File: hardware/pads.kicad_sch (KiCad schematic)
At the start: 0 parts

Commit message: schematic: rx (ESP32-PICO-V3 + SX1281 + Wi-Fi antenna + boot button), blackbox and osd sheets drawn
Co-Authored-By: Claude Opus 5.5 <noreply@anthropic.com>
Claude-Session: https://claude.ai/code/session_01RFaS5jnC9tnPam9GBgmGnG
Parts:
- added D7: TPD2EUSB30, lib:TI_SOT-9X3-3_DRT, symbol lib:TPD2EUSB30DRTR
- added H1, H2, H3: MountingHole 3.5, lib:MountingHole_3.5mm_Ear_Flange5.2, symbol Mechanical:MountingHole
- added J10: M3, lib:MotorPad_PicoBlade_1x03_P1.25mm_PTH0.5, symbol lib:Molex_53047-0310
- added J13: M4, lib:MotorPad_PicoBlade_1x03_P1.25mm_PTH0.5, symbol lib:Molex_53047-0310
- added J16: TP0, lib:SolderPad_1.0x1.2mm, symbol Connector_Generic:Conn_01x01
- added J17: RP0, lib:SolderPad_1.0x1.2mm, symbol Connector_Generic:Conn_01x01
- added J18, J24: 5V, lib:SolderPad_1.0x1.2mm, symbol Connector_Generic:Conn_01x01
- added J19, J25, J27: GND, lib:SolderPad_1.0x1.2mm, symbol Connector_Generic:Conn_01x01
- added J2: +, lib:BattPad_3.0x2.0mm_PTH1.1, symbol Connector_Generic:Conn_01x01
- added J20: LED, lib:SolderPad_1.0x1.2mm_Dense, symbol Connector_Generic:Conn_01x01
- added J21: 5V, lib:SolderPad_1.0x1.2mm_Dense, symbol Connector_Generic:Conn_01x01
- added J22: BZ-, lib:SolderPad_1.0x1.2mm_Dense, symbol Connector_Generic:Conn_01x01
- added J23: CAM, lib:SolderPad_1.0x1.2mm, symbol Connector_Generic:Conn_01x01
- added J26: VHD, lib:SolderPad_1.0x1.2mm, symbol Connector_Generic:Conn_01x01
- added J28: TX1, lib:SolderPad_1.0x1.2mm, symbol Connector_Generic:Conn_01x01
- added J29: RX1, lib:SolderPad_1.0x1.2mm, symbol Connector_Generic:Conn_01x01
- added J3: -, lib:BattPad_3.0x2.0mm_PTH1.1, symbol Connector_Generic:Conn_01x01
- added J31: USB, lib:CONN-SMD_4P-P1.00_BM04B-SRSS-TB, symbol lib:BM04B-SRSS-TB
- added J32: CAM, lib:JST_SUR_SM03B-SURS-TF_1x03-1MP_P0.80mm_Horizontal, symbol lib:SM03B-SURS-TF
- added J33: GND, lib:SolderPad_1.0x1.2mm_Dense, symbol Connector_Generic:Conn_01x01
- added J4: M1, lib:MotorPad_PicoBlade_1x03_P1.25mm_PTH0.5, symbol lib:Molex_53047-0310
- added J7: M2, lib:MotorPad_PicoBlade_1x03_P1.25mm_PTH0.5, symbol lib:Molex_53047-0310
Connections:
- new net +5V: J18.1 (Pin_1), J21.1 (Pin_1)
- new net +5V_CAM: J24.1 (Pin_1), J32.3
- new net +5V_HD: J26.1 (Pin_1)
- new net +BATT_IN: J2.1 (Pin_1)
- new net BUZZER-: J22.1 (Pin_1)
- new net GND: D7.3 (GND), J19.1 (Pin_1), J25.1 (Pin_1), J27.1 (Pin_1), J3.1 (Pin_1), J31.1, J31.5 (MP), J31.6 (MP), J32.2, J32.4 (MP), J32.5 (MP), J33.1 (Pin_1)
- new net LED_STRIP: J20.1 (Pin_1)
- new net M1_A: J4.3
- new net M1_B: J4.2
- new net M1_C: J4.1
- new net M2_A: J7.3
- new net M2_B: J7.2
- new net M2_C: J7.1
- new net M3_A: J10.3
- new net M3_B: J10.2
- new net M3_C: J10.1
- new net M4_A: J13.3
- new net M4_B: J13.2
- new net M4_C: J13.1
- new net PIOUART0_RX: J17.1 (Pin_1)
- new net PIOUART0_TX: J16.1 (Pin_1)
- new net UART1_RX: J29.1 (Pin_1)
- new net UART1_TX: J28.1 (Pin_1)
- new net USB_D_N: D7.2 (D-), J31.2
- new net USB_D_P: D7.1 (D+), J31.3
- new net VBUS: J31.4
- new net VIDEO_IN: J23.1 (Pin_1), J32.1
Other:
- note added: "Battery pads (1S)"
- note added: "Camera pads + JST SUR 0.8 mm plug"
- note added: "HD pads (DJI O4 Lite)"
- note added: "LED strip + buzzer row"
- note added: "Motor lands M1-M4: plug-ready, Molex PicoBlade header DNP"
- note added: "Mounting holes"
- note added: "USB: JST SH 1.0 mm 4-pin + ESD"
- note added: "User UART pads (PIOUART0)"

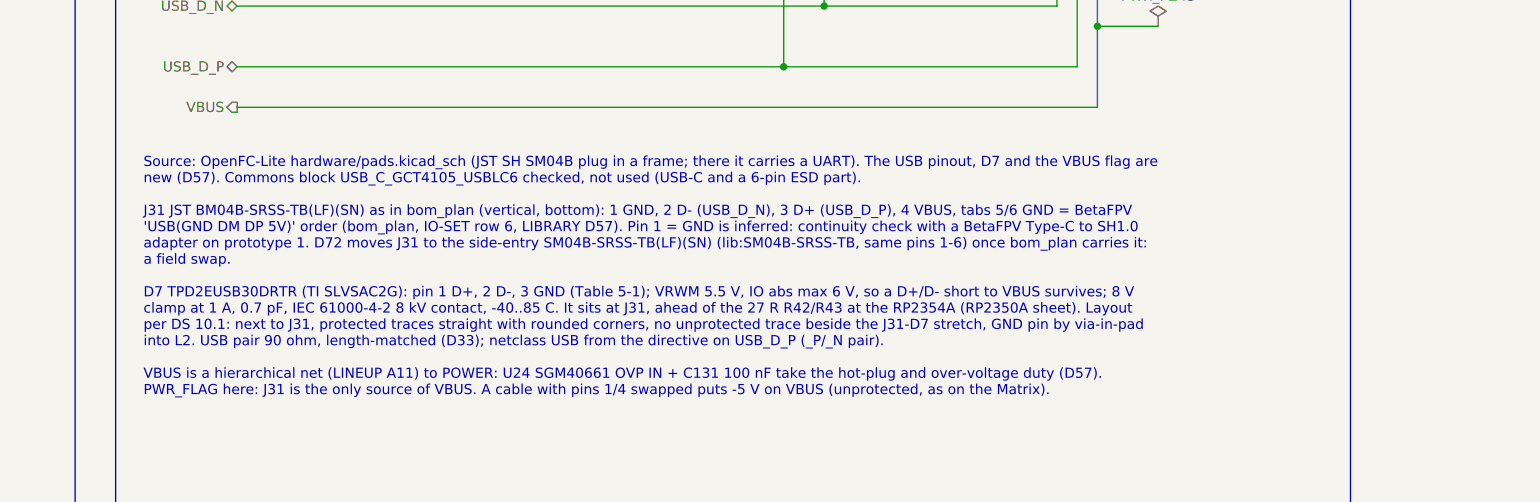
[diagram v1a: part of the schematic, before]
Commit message: wip: schematic integration in progress (saved after container restart)
Co-Authored-By: Claude Opus 5.5 <noreply@anthropic.com>
Claude-Session: https://claude.ai/code/session_01RFaS5jnC9tnPam9GBgmGnG
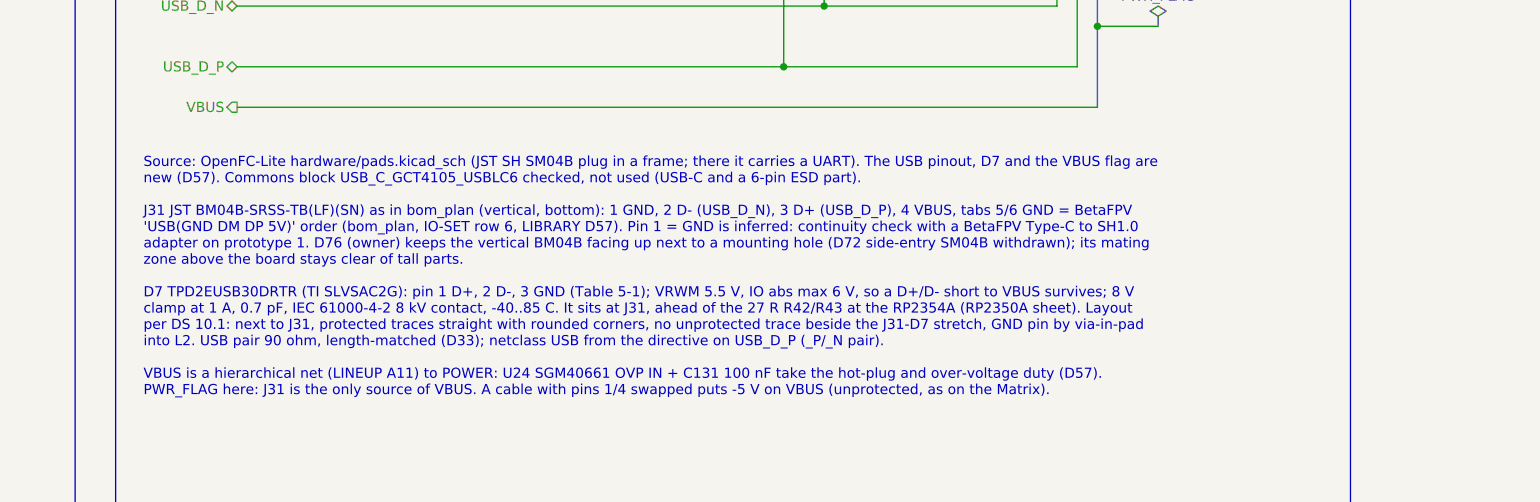
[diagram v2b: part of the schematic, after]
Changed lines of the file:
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@@
 		)
 	)
-	(text_box "Source: OpenFC-Lite hardware/pads.kicad_sch (JST SH SM04B plug in a frame; there it carries a UART). The USB pinout, D7 and the VBUS flag are new (D57). Commons block USB_C_GCT4105_USBLC6 checked, not used (USB-C and a 6-pin ESD part).\n\nJ31 JST BM04B-SRSS-TB(LF)(SN) as in bom_plan (vertical, bottom): 1 GND, 2 D- (USB_D_N), 3 D+ (USB_D_P), 4 VBUS, tabs 5/6 GND = BetaFPV 'USB(GND DM DP 5V)' order (bom_plan, IO-SET row 6, LIBRARY D57). Pin 1 = GND is inferred: continuity check with a BetaFPV Type-C to SH1.0 adapter on prototype 1. D72 moves J31 to the side-entry SM04B-SRSS-TB(LF)(SN) (lib:SM04B-SRSS-TB, same pins 1-6) once bom_plan carries it: a field swap.\n\nD7 TPD2EUSB30DRTR (TI SLVSAC2G): pin 1 D+, 2 D-, 3 GND (Table 5-1); VRWM 5.5 V, IO abs max 6 V, so a D+/D- short to VBUS survives; 8 V clamp at 1 A, 0.7 pF, IEC 61000-4-2 8 kV contact, -40..85 C. It sits at J31, ahead of the 27 R R42/R43 at the RP2354A (RP2350A sheet). Layout per DS 10.1: next to J31, protected traces straight with rounded corners, no unprotected trace beside the J31-D7 stretch, GND pin by via-in-pad into L2. USB pair 90 ohm, length-matched (D33); netclass USB from the directive on USB_D_P (_P/_N pair).\n\nVBUS is a hierarchical net (LINEUP A11) to POWER: U24 SGM40661 OVP IN + C131 100 nF take the hot-plug and over-voltage duty (D57). PWR_FLAG here: J31 is the only source of VBUS. A cable with pins 1/4 swapped puts -5 V on VBUS (unprotected, as on the Matrix)."
+	(text_box "Source: OpenFC-Lite hardware/pads.kicad_sch (JST SH SM04B plug in a frame; there it carries a UART). The USB pinout, D7 and the VBUS flag are new (D57). Commons block USB_C_GCT4105_USBLC6 checked, not used (USB-C and a 6-pin ESD part).\n\nJ31 JST BM04B-SRSS-TB(LF)(SN) as in bom_plan (vertical, bottom): 1 GND, 2 D- (USB_D_N), 3 D+ (USB_D_P), 4 VBUS, tabs 5/6 GND = BetaFPV 'USB(GND DM DP 5V)' order (bom_plan, IO-SET row 6, LIBRARY D57). Pin 1 = GND is inferred: continuity check with a BetaFPV Type-C to SH1.0 adapter on prototype 1. D76 (owner) keeps the vertical BM04B facing up next to a mounting hole (D72 side-entry SM04B withdrawn); its mating zone above the board stays clear of tall parts.\n\nD7 TPD2EUSB30DRTR (TI SLVSAC2G): pin 1 D+, 2 D-, 3 GND (Table 5-1); VRWM 5.5 V, IO abs max 6 V, so a D+/D- short to VBUS survives; 8 V clamp at 1 A, 0.7 pF, IEC 61000-4-2 8 kV contact, -40..85 C. It sits at J31, ahead of the 27 R R42/R43 at the RP2354A (RP2350A sheet). Layout per DS 10.1: next to J31, protected traces straight with rounded corners, no unprotected trace beside the J31-D7 stretch, GND pin by via-in-pad into L2. USB pair 90 ohm, length-matched (D33); netclass USB from the directive on USB_D_P (_P/_N pair).\n\nVBUS is a hierarchical net (LINEUP A11) to POWER: U24 SGM40661 OVP IN + C131 100 nF take the hot-plug and over-voltage duty (D57). PWR_FLAG here: J31 is the only source of VBUS. A cable with pins 1/4 swapped puts -5 V on VBUS (unprotected, as on the Matrix)."
 		(exclude_from_sim no)
 		(at 254 73.66 0)
@@
 		(in_pos_files no)
 		(dnp no)
-		(property "Reference" "#PWR1407"
+		(property "Reference" "#PWR238"
 			(at 60.96 158.75 0)
 			(hide yes)
@@
 			(project "OpenAIO-Whoop"
 				(path "/2c3a7206-1e66-4d43-a02f-491225e20dd6/8d214749-72cf-5803-99b7-260f0c3f1838"
-					(reference "#PWR1407")
+					(reference "#PWR238")
 					(unit 1)
 				)
@@
 		(in_pos_files no)
 		(dnp no)
-		(property "Reference" "#PWR1403"
+		(property "Reference" "#PWR234"
 			(at 367.03 49.53 0)
 			(hide yes)
@@
 			(project "OpenAIO-Whoop"
 				(path "/2c3a7206-1e66-4d43-a02f-491225e20dd6/8d214749-72cf-5803-99b7-260f0c3f1838"
-					(reference "#PWR1403")
+					(reference "#PWR234")
 					(unit 1)
 				)
@@
 		(in_pos_files no)
 		(dnp no)
-		(property "Reference" "#PWR1409"
+		(property "Reference" "#PWR240"
 			(at 137.16 148.59 0)
 			(hide yes)
@@
 			(project "OpenAIO-Whoop"
 				(path "/2c3a7206-1e66-4d43-a02f-491225e20dd6/8d214749-72cf-5803-99b7-260f0c3f1838"
-					(reference "#PWR1409")
+					(reference "#PWR240")
 					(unit 1)
 				)
@@
 		(in_pos_files no)
 		(dnp no)
-		(property "Reference" "#PWR1415"
+		(property "Reference" "#PWR245"
 			(at 325.12 148.59 0)
 			(hide yes)
@@
 			(project "OpenAIO-Whoop"
 				(path "/2c3a7206-1e66-4d43-a02f-491225e20dd6/8d214749-72cf-5803-99b7-260f0c3f1838"
-					(reference "#PWR1415")
+					(reference "#PWR245")
 					(unit 1)
 				)
@@
 		(in_pos_files no)
 		(dnp no)
-		(property "Reference" "#PWR1410"
+		(property "Reference" "#PWR241"
 			(at 215.9 158.75 0)
 			(hide yes)
@@
 			(project "OpenAIO-Whoop"
 				(path "/2c3a7206-1e66-4d43-a02f-491225e20dd6/8d214749-72cf-5803-99b7-260f0c3f1838"
-					(reference "#PWR1410")
+					(reference "#PWR241")
 					(unit 1)
 				)
@@
 		(in_pos_files no)
 		(dnp no)
-		(property "Reference" "#PWR1411"
+		(property "Reference" "#PWR242"
 			(at 226.06 148.59 0)
 			(hide yes)
@@
 			(project "OpenAIO-Whoop"
 				(path "/2c3a7206-1e66-4d43-a02f-491225e20dd6/8d214749-72cf-5803-99b7-260f0c3f1838"
-					(reference "#PWR1411")
+					(reference "#PWR242")
 					(unit 1)
 				)
@@
 		(in_pos_files no)
 		(dnp no)
-		(property "Reference" "#PWR1406"
+		(property "Reference" "#PWR237"
 			(at 50.8 148.59 0)
 			(hide yes)
@@
 			(project "OpenAIO-Whoop"
 				(path "/2c3a7206-1e66-4d43-a02f-491225e20dd6/8d214749-72cf-5803-99b7-260f0c3f1838"
-					(reference "#PWR1406")
+					(reference "#PWR237")
 					(unit 1)
 				)
@@
 		(in_pos_files no)
 		(dnp no)
-		(property "Reference" "#PWR1412"
+		(property "Reference" "#PWR243"
 			(at 254 158.75 0)
 			(hide yes)
@@
 			(project "OpenAIO-Whoop"
 				(path "/2c3a7206-1e66-4d43-a02f-491225e20dd6/8d214749-72cf-5803-99b7-260f0c3f1838"
-					(reference "#PWR1412")
+					(reference "#PWR243")
 					(unit 1)
 				)
@@
 		(in_pos_files no)
 		(dnp no)
-		(property "Reference" "#FLG1401"
+		(property "Reference" "#FLG08"
 			(at 382.27 56.515 0)
 			(hide yes)
@@
 			(project "OpenAIO-Whoop"
 				(path "/2c3a7206-1e66-4d43-a02f-491225e20dd6/8d214749-72cf-5803-99b7-260f0c3f1838"
-					(reference "#FLG1401")
+					(reference "#FLG08")
 					(unit 1)
 				)
@@
 		(in_pos_files no)
 		(dnp no)
-		(property "Reference" "#PWR1405"
+		(property "Reference" "#PWR233"
 			(at 347.98 49.53 0)
 			(hide yes)
@@
 			(project "OpenAIO-Whoop"
 				(path "/2c3a7206-1e66-4d43-a02f-491225e20dd6/8d214749-72cf-5803-99b7-260f0c3f1838"
-					(reference "#PWR1405")
+					(reference "#PWR233")
 					(unit 1)
 				)
@@
 		(in_pos_files no)
 		(dnp no)
-		(property "Reference" "#PWR1414"
+		(property "Reference" "#PWR244"
 			(at 260.35 158.75 0)
 			(hide yes)
@@
 			(project "OpenAIO-Whoop"
 				(path "/2c3a7206-1e66-4d43-a02f-491225e20dd6/8d214749-72cf-5803-99b7-260f0c3f1838"
-					(reference "#PWR1414")
+					(reference "#PWR244")
 					(unit 1)
 				)
@@
 		(in_pos_files no)
 		(dnp no)
-		(property "Reference" "#PWR1416"
+		(property "Reference" "#PWR246"
 			(at 335.28 158.75 0)
 			(hide yes)
@@
 			(project "OpenAIO-Whoop"
 				(path "/2c3a7206-1e66-4d43-a02f-491225e20dd6/8d214749-72cf-5803-99b7-260f0c3f1838"
-					(reference "#PWR1416")
+					(reference "#PWR246")
 					(unit 1)
 				)
@@
 		(in_pos_files no)
 		(dnp no)
-		(property "Reference" "#PWR1401"
+		(property "Reference" "#PWR236"
 			(at 30.48 41.91 0)
 			(hide yes)
@@
 			(project "OpenAIO-Whoop"
 				(path "/2c3a7206-1e66-4d43-a02f-491225e20dd6/8d214749-72cf-5803-99b7-260f0c3f1838"
-					(reference "#PWR1401")
+					(reference "#PWR236")
 					(unit 1)
 				)
@@
 		(in_pos_files no)
 		(dnp no)
-		(property "Reference" "#PWR1404"
+		(property "Reference" "#PWR235"
 			(at 379.73 49.53 0)
 			(hide yes)
@@
 			(project "OpenAIO-Whoop"
 				(path "/2c3a7206-1e66-4d43-a02f-491225e20dd6/8d214749-72cf-5803-99b7-260f0c3f1838"
-					(reference "#PWR1404")
+					(reference "#PWR235")
 					(unit 1)
 				)
@@
 		(in_pos_files no)
 		(dnp no)
-		(property "Reference" "#PWR1408"
+		(property "Reference" "#PWR239"
 			(at 116.84 158.75 0)
 			(hide yes)
@@
 			(project "OpenAIO-Whoop"
 				(path "/2c3a7206-1e66-4d43-a02f-491225e20dd6/8d214749-72cf-5803-99b7-260f0c3f1838"
-					(reference "#PWR1408")
+					(reference "#PWR239")
 					(unit 1)
 				)
@@
 		(in_pos_files no)
 		(dnp no)
-		(property "Reference" "#PWR1413"
+		(property "Reference" "#PWR247"
 			(at 256.54 153.67 0)
 			(hide yes)
@@
 			(project "OpenAIO-Whoop"
 				(path "/2c3a7206-1e66-4d43-a02f-491225e20dd6/8d214749-72cf-5803-99b7-260f0c3f1838"
-					(reference "#PWR1413")
+					(reference "#PWR247")
 					(unit 1)
 				)
@@
 		(in_pos_files no)
 		(dnp no)
-		(property "Reference" "#PWR1402"
+		(property "Reference" "#PWR232"
 			(at 53.34 49.53 0)
 			(hide yes)
@@
 			(project "OpenAIO-Whoop"
 				(path "/2c3a7206-1e66-4d43-a02f-491225e20dd6/8d214749-72cf-5803-99b7-260f0c3f1838"
-					(reference "#PWR1402")
+					(reference "#PWR232")
 					(unit 1)
 				)

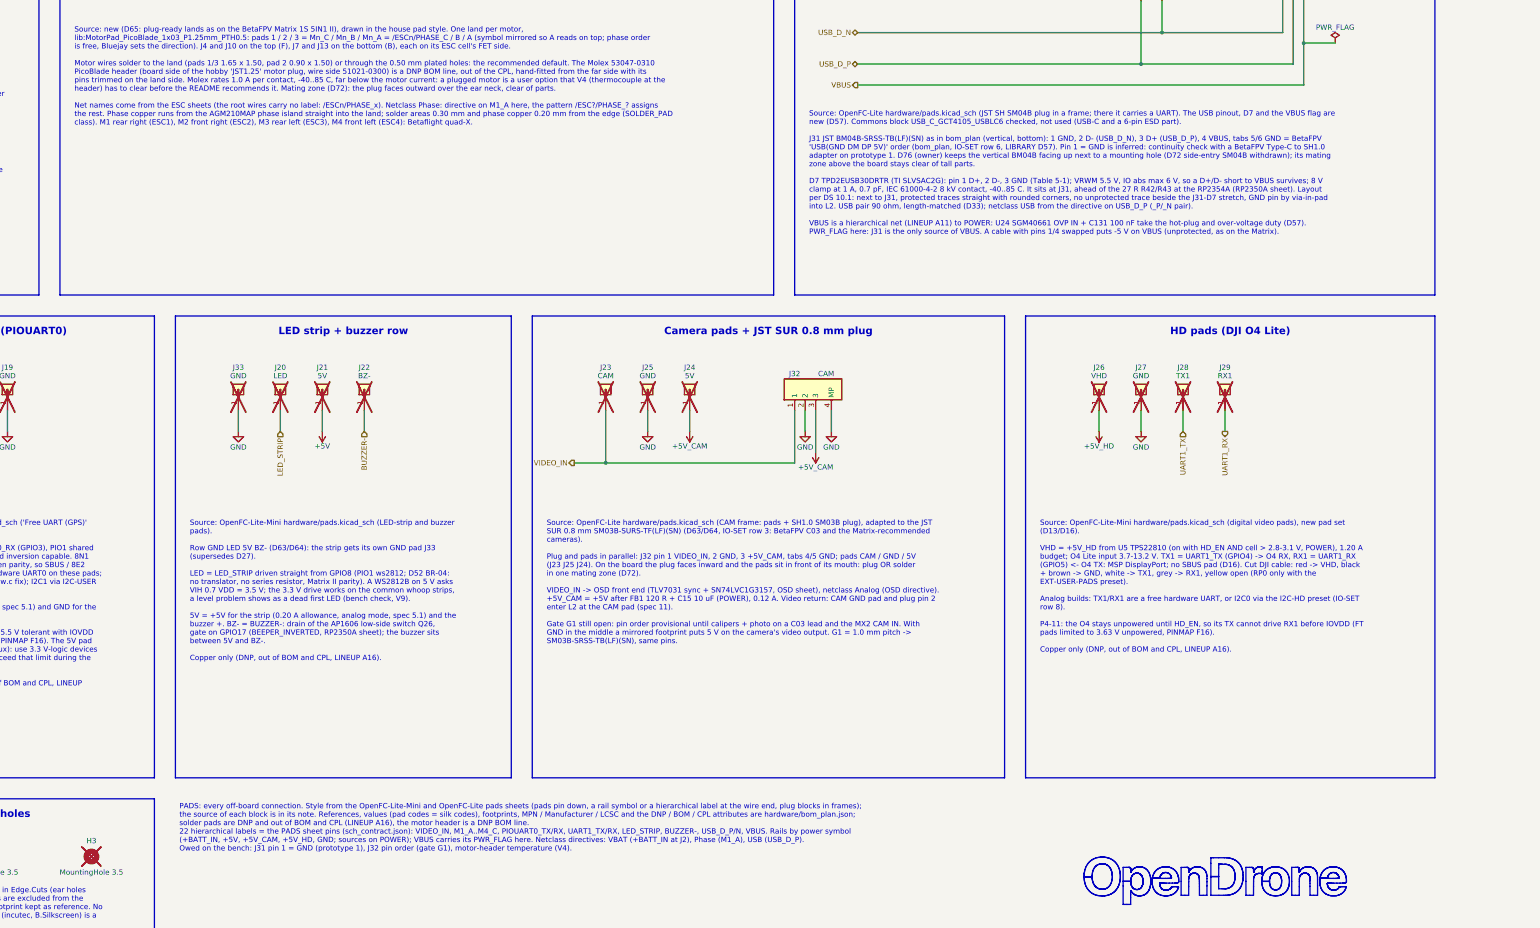
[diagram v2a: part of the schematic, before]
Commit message: schematic: integrated (ERC 0 errors / 2 justified warnings; check_netlist 7/7; conventions 0 FAIL; visual 0 hits; 268/268 refs match bom_plan; FC+RX pin maps match PINMAP)
Co-Authored-By: Claude Opus 5.5 <noreply@anthropic.com>
Claude-Session: https://claude.ai/code/session_01RFaS5jnC9tnPam9GBgmGnG
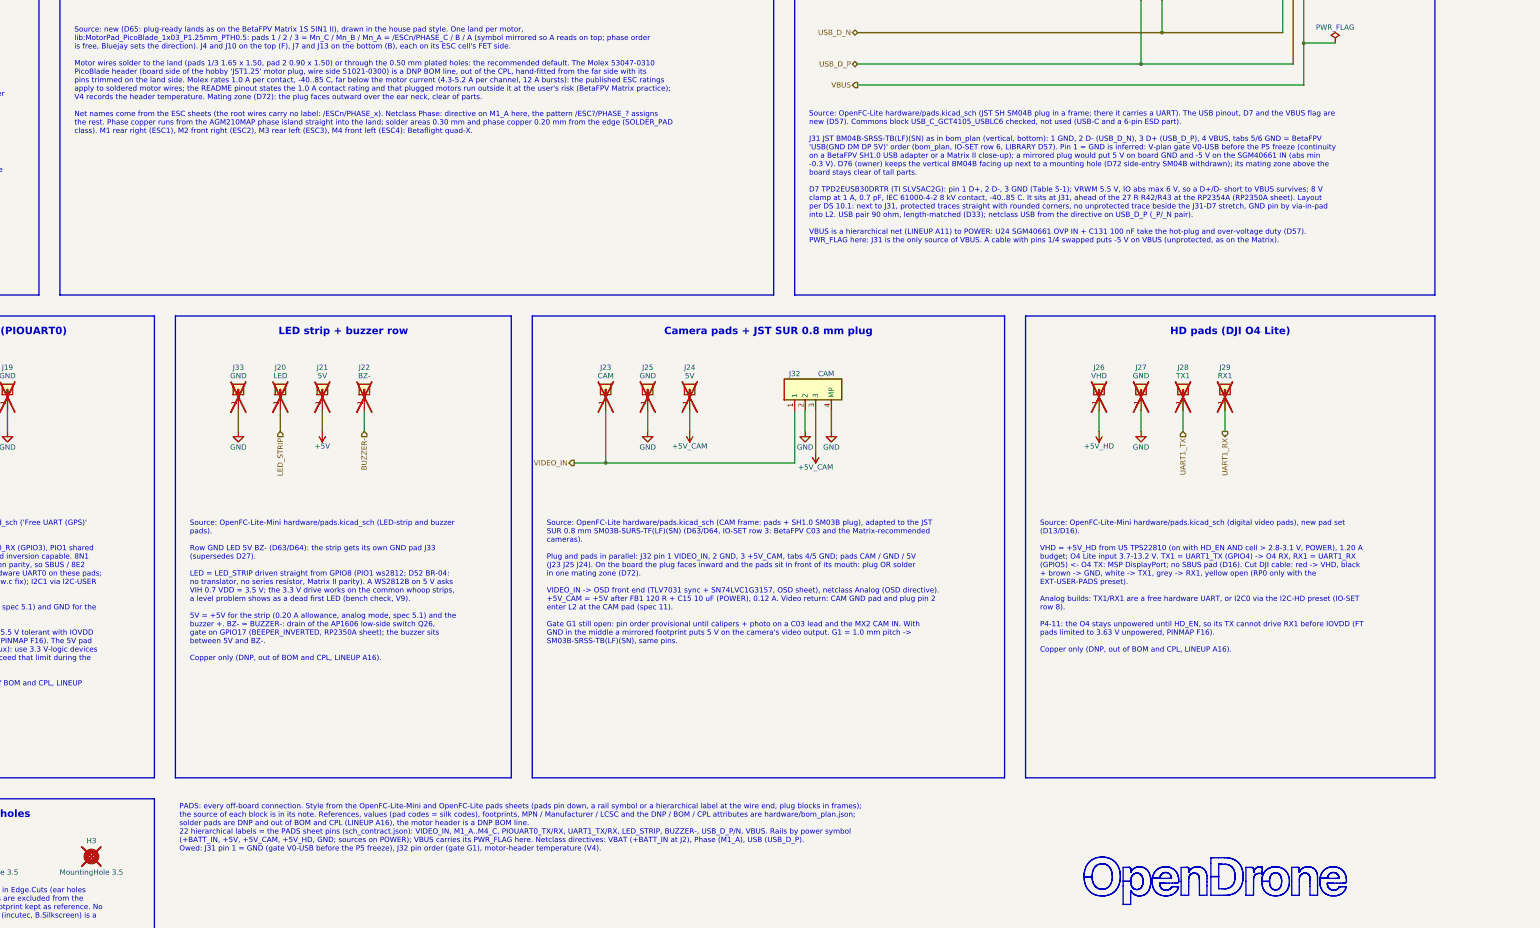
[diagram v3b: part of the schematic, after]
